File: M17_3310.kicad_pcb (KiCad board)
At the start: 4 copper layers, 41.4 x 108 mm, 113 parts, among them J1 SWD_DBG, J2 ANT_A, J3 ANT_B, J4 Battery, J7 Display, J8 USB C, Q1 BSS138, Q2 IRLML6401, Q3 BSS138, Q4 BSS138, Q5 BSS84, Q6 BSS138, Q7 BSS138, Q8 IRLML6401, Q9 BSS138, SW1 POWER ON, SW2 "OK", U1 STM32F405RGTx, U2 SA868, U3 MAX1555, U4 TPS63030DSK, U5 USBLC6-2SC6, Y1 8MHz

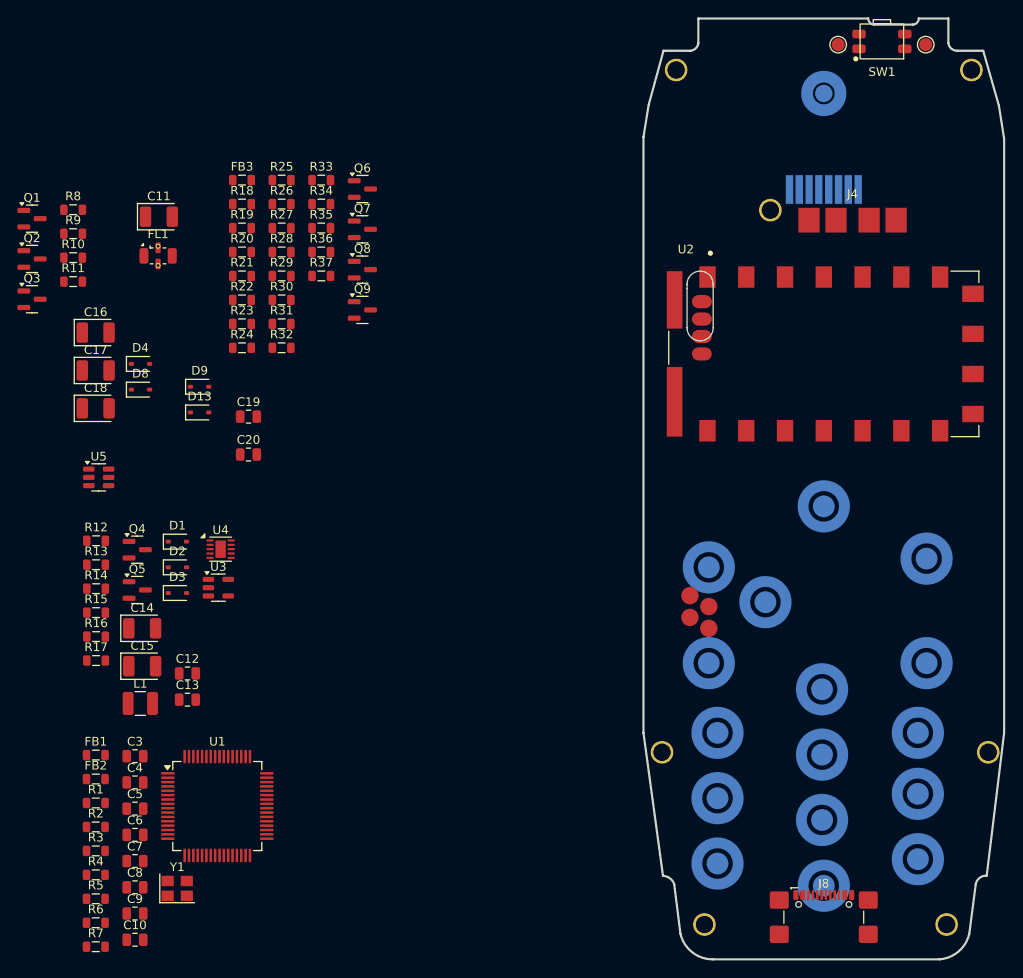
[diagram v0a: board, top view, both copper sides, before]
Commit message: keypad in place
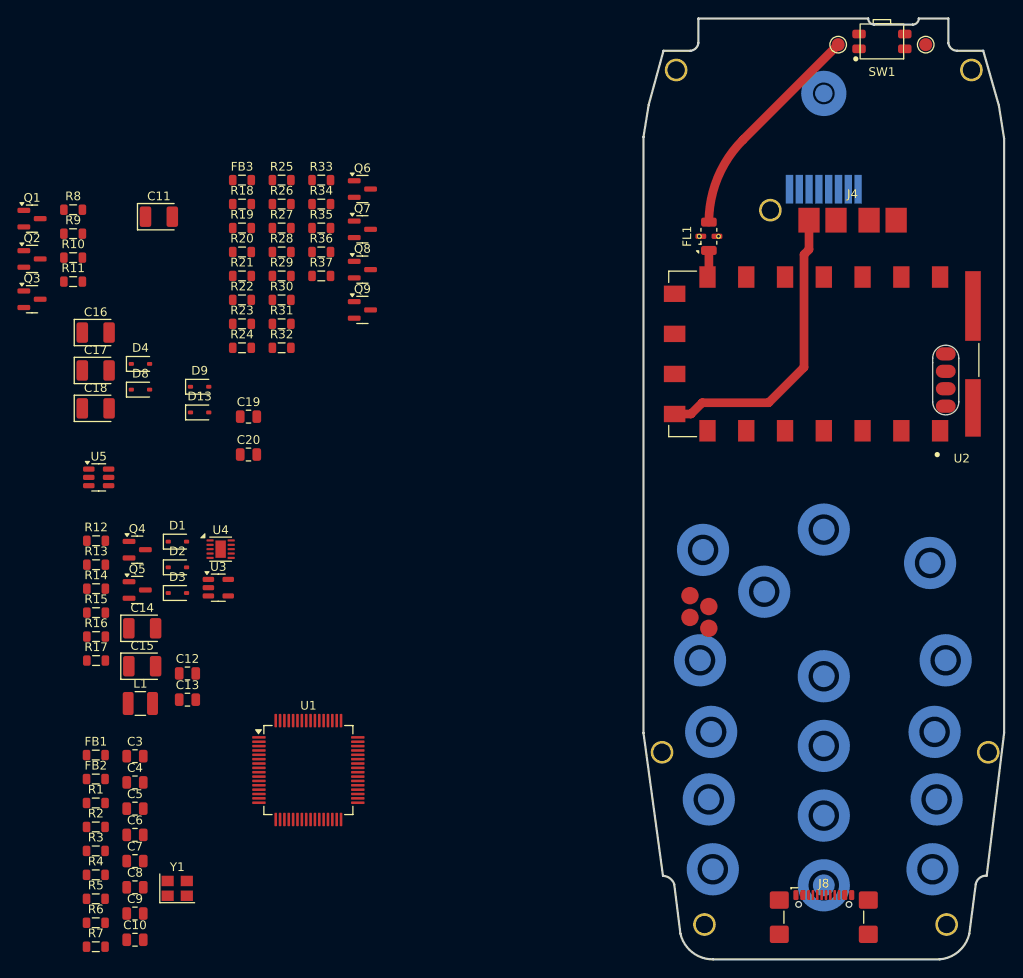
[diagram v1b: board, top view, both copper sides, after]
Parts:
- moved FL1 63.3 mm to (127.5, 67.0), turned to 90 degrees
- moved SW4 27.2 mm to (154.7, 115.7)
- moved SW14 26.0 mm to (126.5, 115.7)
- moved SW5 24.9 mm to (153.4, 123.9)
- moved SW15 23.7 mm to (127.8, 123.9)
- moved U1 11.2 mm to (81.5, 128.3)
- moved SW13 9.34 mm to (126.8, 103.0)
- moved SW8 6.95 mm to (133.9, 107.8)
- moved SW2 2.67 mm to (140.7, 100.7)
- moved SW6 2.24 mm to (153.7, 131.6)
- moved SW7 2.04 mm to (153.2, 139.7)
- moved SW9 1.51 mm to (140.7, 117.5)
- moved SW10 1.02 mm to (140.7, 125.5)
- moved SW16 1.01 mm to (127.5, 131.6)
- moved SW17 0.85 mm to (128.0, 139.7)
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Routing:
- net /PMU/U_BATT: track 0.00 -> 34.2 mm
- net Net-(FL1-OUT): track 0.00 -> 25.9 mm
- net Net-(FL1-IN): track 0.00 -> 3.12 mm
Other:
- outline, holes or cut-outs redrawn
